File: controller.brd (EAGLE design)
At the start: 150 x 100 mm, 0 parts

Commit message: Firmware added, controller progress
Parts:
- added C1, C2: 18pF, rcl:C0603
- added C10, C11, C12, C18, C19, C20, C21, C22, C3, C4, C5, C6, C7, C8, C9: 0.1µF, rcl:C0603
- added C13, C14, C15: 100µF, rcl:PANASONIC_D
- added C16, C17: 10µF, rcl:C0805
- added J1: SATA0010225X, BW-Connectors:SATA0010225X
- added J10: ALED_A, BW-Connectors:B3B-XH-A
- added J11: ALED_B, BW-Connectors:B3B-XH-A
- added J12: ALED_C, BW-Connectors:B3B-XH-A
- added J13: FRONT_PANEL, pinhead:1X05
- added J14: 12V, pinhead:2X05
- added J15: 5V, pinhead:2X10
- added J16: 3.3V, pinhead:2X02
- added J2: USB, pinhead:1X04
- added J3: ICSP, BW-Connectors:5PIN-1.27
- added J4: PUMP, BW-Connectors:47053-1000
- added J5: FANS, BW-Connectors:47053-1000
- added J6: FLOW, BW-Connectors:22-23-2032
- added J7: TEMP, pinhead:1X02
- added J8: TACH_OUT, BW-Connectors:22-23-2032
- added J9: SHUTDOWN, pinhead:1X02
- added LS1: AI-1224-TWT-5V-R, BW-Active:AI-1224-TWT-5V-R
- added Q1, Q2, Q3, Q4, Q5, Q6, Q7, Q8: NMOSL, BW-Active:SOT23
- added R1, R10, R13, R15: 10kΩ, resistor:R0603
- added R11, R6: 4.7kΩ, resistor:R0603
- added R12, R14, R3, R4: ?, resistor:R0603
- added R2, R5: 1kΩ, resistor:R0603
- added R7, R8, R9: 100kΩ, resistor:R0603
- added SJ1: GNDLINK, jumper:SJ
- added SW1: RESET, BW-PassiveMechanical:TL3305_MICROSWITCH
- added U1: PIC32MZ-EF-144, BW-Active:LQFP144-20X20
- added U2: NCP5501DT33, BW-Active:DPAK
- added U3: MAX6071A_30, BW-Active:SOT23-6L
- added U4: TXU0104, BW-Active:TSSOP14
- added U5: CPC1006N, BW-Active:CPC1006N
- added Y1: 24MHz, BW-PassiveMechanical:HC49/4HSMX
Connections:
- new net !MCLR: J3.1, R2.1, U1.20
- new net !MCLR!_FILTER: C3.1, R1.1, R2.2, SW1.1, SW1.2
- new net 12V: C15.+, J1.P13, J1.P14, J1.P15, J14.1, J14.3, J14.5, J14.7, J14.9, J4.2, J5.2
- new net 3.3V: C10.1, C11.1, C12.1, C13.+, C17.1, C21.1, C4.1, C5.1, C6.1, C7.1, C8.1, C9.1, J16.1, J16.3, J3.2, R1.2, U1.107, U1.122, U1.137, U1.18, U1.33, U1.41, U1.55, U1.64, U1.74, U1.88, U2.3, U4.1
- new net 3V_REF: C20.1, R6.2, U1.40, U3.5, U3.6
- new net 5V: C14.+, C22.1, J1.P7, J1.P8, J1.P9, J10.3, J11.3, J12.3, J15.1, J15.11, J15.13, J15.15, J15.17, J15.19, J15.3, J15.5, J15.7, J15.9, J6.2, LS1.+, R10.2, R11.2, R12.1, R13.2, R14.1, R15.2, R5.2, U4.14
- new net 5V_USB: C16.1, C19.1, J13.1, J2.1, R7.2, R8.2, R9.2, U1.73, U2.1, U3.3, U3.4
- new net ALED_A: J10.2, U4.13
- new net ALED_A_RAW: U1.104, U4.2
- new net ALED_B: J11.2, U4.12
- new net ALED_B_RAW: U1.109, U4.3
- new net ALED_C: J12.2, U4.11
- new net ALED_C_RAW: U1.110, U4.4
- new net ALED_OE: U1.103, U4.8
- new net BUZZER_EN: Q2.1, U1.9
- new net BUZZER_L: LS1.-, Q2.3
- new net EMERGENCY_SD_C1: J9.1, U5.4
- new net EMERGENCY_SD_C2: J9.2, U5.3
- new net EMERGENCY_SD_DRIVE+: R11.1, U5.1
- new net EMERGENCY_SD_DRIVE-: Q8.3, U5.2
- new net EMERGENCY_SD_TRIGGER: Q8.1, U1.10
- new net FAN_PWM: J5.4, Q6.3, R14.2
- new net FAN_PWM_DRIVE: Q6.1, U1.15
- new net FAN_TACH: Q7.3, U1.16
- new net FAN_TACH_RAW: J5.3, Q7.1, R15.1
- new net FLOW_TACH: Q1.3, U1.23
- new net FLOW_TACH_RAW: J6.3, Q1.1, R10.1
- new net FPLED_!B: J13.4, R9.1, U1.98
- new net FPLED_!G: J13.3, R8.1, U1.97
- new net FPLED_!R: J13.2, R7.1, U1.96
- new net GND: C1.1, C10.2, C11.2, C12.2, C13.-, C14.-, C15.-, C16.2, C17.2, C18.2, C19.2, C2.1, C20.2, C21.2, C22.2, C3.2, C4.2, C5.2, C6.2, C7.2, C8.2, C9.2, J1.P10, J1.P12, J1.P4, J1.P5, J1.P6, J10.1, J11.1, J12.1, J13.5, J14.10, J14.2, J14.4, J14.6, J14.8, J15.10, J15.12, J15.14, J15.16, J15.18, J15.2, J15.20, J15.4, J15.6, J15.8, J16.2, J16.4, J2.4, J3.3, J4.1, J5.1, J6.1, J7.2, Q1.2, Q2.2, Q3.2, Q4.2, Q5.2, Q6.2, Q7.2, Q8.2, SJ1.2, SW1.3, SW1.4, U1.108, U1.123, U1.136, U1.17, U1.32, U1.42, U1.54, U1.63, U1.75, U1.89, U2.TAB, U3.1, U3.2, U4.7
- new net OSC1: C2.2, R3.2, U1.71, Y1.2
- new net OSC2: R4.1, U1.72
- new net OSC2_R: C1.2, R3.1, R4.2, Y1.1
- new net PGEC: J3.5, U1.35
- new net PGED: J3.4, U1.36
- new net POWER_SENSE: R5.1, U1.46
- new net PUMP_PWM: J4.4, Q4.3, R12.2
- new net PUMP_PWM_DRIVE: Q4.1, U1.12
- new net PUMP_TACH: Q5.3, U1.14
- new net PUMP_TACH_RAW: J4.3, Q5.1, R13.1
- new net TACH_OUT: J8.3, Q3.3
- new net TACH_OUT_DRIVE: Q3.1, U1.11
- new net TACH_OUT_GNDLINK: J8.1, SJ1.1
- new net TEMP_SENSE: C18.1, J7.1, R6.1, U1.25
- new net USB_D+: J2.3, U1.77
- new net USB_D-: J2.2, U1.76

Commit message: Controller (hopefully) finished
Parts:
- added A1: VXO7805-500, BW-Active:VXO78-500
- added C23, C27: 0.1µF, rcl:C0603
- added C24: 22µF, rcl:C0603
- added C25: 10µF, rcl:C0805
- added C26: 100µF, rcl:PANASONIC_D
- added D1, D2: GS1A-L, BW-Active:DO-214AC
- added J17: 12V_WD, pinhead:1X02
- added K1: G5Q-1, BW-PassiveMechanical:G5Q-1
- added Q10, Q9: PMOS, BW-Active:SOT23
- added Q11: NMOSL, BW-Active:SOT23
- added R16, R18: 1kΩ, resistor:R0603
- added R17: 10kΩ, resistor:R0603
- added TP1, TP10, TP11, TP12, TP14, TP15, TP2, TP3, TP4, TP5, TP6, TP7, TP8, TP9: RCU-0(J), BW-PassiveMechanical:TP_0603_JOINED
- moved Q8 536.6 mm to (73.8, 58.7), flipped to the bottom, turned to 180 degrees
- moved J15 517.1 mm to (14.6, 59.7), turned to 180 degrees
- moved R15 504.1 mm to (38.9, 58.5), flipped to the bottom, turned to 270 degrees
- moved J14 504.0 mm to (20.0, 53.5), turned to 180 degrees
- moved Q7 501.0 mm to (41.7, 62.1), flipped to the bottom, turned to 90 degrees
- moved R14 490.3 mm to (45.5, 57.5), flipped to the bottom, turned to 90 degrees
- moved Q6 487.0 mm to (45.8, 61.2), flipped to the bottom
- moved R13 476.0 mm to (50.2, 56.1), flipped to the bottom, turned to 180 degrees
- moved J16 474.1 mm to (15.0, 14.5)
- moved Q5 465.3 mm to (46.9, 53.0), flipped to the bottom, turned to 270 degrees
- moved SJ1 463.7 mm to (70.2, 65.6), turned to 180 degrees
- moved R12 462.2 mm to (50.2, 56.1), turned to 180 degrees
- moved Q4 453.3 mm to (46.6, 54.9)
- moved R11 441.8 mm to (78.5, 54.7), turned to 270 degrees
- moved Q3 440.5 mm to (51.0, 53.0), turned to 270 degrees
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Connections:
- new net 12V_PUMP: J4.2, K1.2
- new net 12V_PUMP_WD: K1.4, Q10.3
- new net 12V_WD: A1.1, C25.1, C26.+, Q10.2, Q9.2, R17.2
- new net 12V_WD_PROTECT: Q9.1, R16.1
- new net 12V_WD_RAW: J17.1, Q9.3
- new net 5V_SB: C16.1, C19.1, D1.C, D2.C, J13.1, R12.1, R13.2, R7.2, R8.2, R9.2, TP5.1, U2.1, U3.3, U3.4
- new net 5V_WD: A1.3, C24.1, D2.A, R18.2
- new net PUMP_WD_DRIVE: Q10.1, Q11.3, R17.1
- new net PUMP_WD_RUN: Q11.1, U1.8
- new net WD_DETECT: R18.1, U1.81
- net 12V: now also K1.1, K1.3; no longer J4.2
- net 3.3V: now also C27.1
- net 3V_REF: now also TP6.1
- net 5V: no longer R12.1, R13.2
- net 5V_USB: now also C23.1, D1.A, TP4.1; no longer C16.1, C19.1, J13.1, R7.2, R8.2, R9.2, U2.1, U3.3, U3.4
- net ALED_A: now also TP1.1
- net ALED_B: now also TP2.1
- net ALED_C: now also TP3.1
- net ALED_OE: now also TP15.1
- net FAN_PWM: now also TP14.1
- net FAN_TACH: now also TP12.1
- net FLOW_TACH: now also TP8.1
- net GND: now also A1.2, C23.2, C24.2, C25.2, C26.-, C27.2, J17.2, K1.5, Q11.2, R16.2
- net PUMP_PWM: now also TP11.1
- net PUMP_TACH: now also TP10.1
- net TACH_OUT: now also TP9.1
- net TEMP_SENSE: now also TP7.1
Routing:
- net 5V: track 0.00 -> 264.4 mm
- net 3.3V: track 0.00 -> 150.2 mm, vias 0 -> 13
- net 5V_SB: track 0.00 -> 141.4 mm, vias 0 -> 8
- net 12V: track 0.00 -> 105.8 mm
- net 12V_WD: track 0.00 -> 75.1 mm, vias 0 -> 5
- net GND: track 0.00 -> 46.9 mm, vias 0 -> 128
- net BUZZER_EN: track 0.00 -> 36.1 mm, vias 0 -> 1
- net EMERGENCY_SD_TRIGGER: track 0.00 -> 35.8 mm, vias 0 -> 1
- net PUMP_WD_RUN: track 0.00 -> 26.2 mm, vias 0 -> 1
- net ALED_OE: track 0.00 -> 24.3 mm, vias 0 -> 1
- net !MCLR: track 0.00 -> 23.8 mm
- net TEMP_SENSE: track 0.00 -> 22.6 mm
- net ALED_B: track 0.00 -> 21.6 mm, vias 0 -> 1
- net TACH_OUT: track 0.00 -> 21.2 mm, vias 0 -> 1
- net FAN_PWM_DRIVE: track 0.00 -> 20.8 mm, vias 0 -> 1
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- added copper zone on layer 1, net GND
- added copper zone on layer 16, net GND
- added copper zone on layer 1, net LOGO
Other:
- board size 150 x 100 mm -> 81 x 70 mm
- board text added: "+"
- board text added: "+ -"
- board text added: "- +"
- board text added: "JLCJLCJLCJLC"
- board text added: "©2022 BlockWorker blockworker.de"

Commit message: Parts Ordered
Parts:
- R11: value 4.7kΩ -> 2kΩ
- U4: value TXU0104 -> TXU0304-3
- U5: value CPC1006N -> CPC1017N; device BW-Active:CPC1006N -> BW-Active:CPC10*N
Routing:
- net GND: vias 128 -> 155
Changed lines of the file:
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@@
 <setting verticaltext="up"/>
 </settings>
-<grid distance="0.02" unitdist="mm" unit="mm" style="lines" multiple="1" display="no" altdistance="0.1" altunitdist="mm" altunit="mm"/>
+<grid distance="1" unitdist="mm" unit="mm" style="lines" multiple="1" display="no" altdistance="0.1" altunitdist="mm" altunit="mm"/>
 <layers>
 <layer number="1" name="Top" color="4" fill="1" visible="yes" active="yes"/>
@@
 </layers>
 <board>
+<fusionsync huburn="a.cGVyc29uYWw6dWUyYmY1N2E4" projecturn="a.cGVyc29uYWw6dWUyYmY1N2E4IzIwMjIwMTIwNDg3Nzg3NTgx" f3durn="urn:adsk.wipprod:dm.lineage:FNo4Y8BsTfObfx8X_7kaJQ" pcbguid="" lastpulledtime="" lastsyncedchangeguid="" latestrevisionid="456a566e-ee09-4212-9d23-57c6c17b9b97" lastsyncedrevisionid="456a566e-ee09-4212-9d23-57c6c17b9b97" lastboardhashguid="7ab29c69-62af-bade-653a-f237d7fa49a6" lastpushedtime="2022-02-19T19:35:36Z" linktopcb3d="true"/>
 <plain>
 <wire x1="0" y1="0" x2="81" y2="0" width="0" layer="20"/>
@@
 <attribute name="VALUE" x="28.065" y="45.195" size="1.016" layer="27" font="vector" ratio="15"/>
 </element>
-<element name="U4" library="BW-Active" library_urn="urn:adsk.eagle:library:33783073" package="TSSOP14" package3d_urn="urn:adsk.eagle:package:33783235/2" value="TXU0104" x="57" y="23.5" smashed="yes" rot="MR90">
+<element name="U4" library="BW-Active" library_urn="urn:adsk.eagle:library:33783073" package="TSSOP14" package3d_urn="urn:adsk.eagle:package:33783235/2" value="TXU0304-3" x="57" y="23.5" smashed="yes" rot="MR90">
 <attribute name="NAME" x="55.6828" y="19.5956" size="1.016" layer="26" font="vector" ratio="15" rot="MR0"/>
 <attribute name="VALUE" x="60.1828" y="26.4138" size="1.016" layer="28" font="vector" ratio="15" rot="MR0"/>
@@
 <attribute name="VALUE" x="69.925" y="33.895" size="1.016" layer="28" font="vector" ratio="15" rot="MR90"/>
 </element>
-<element name="U5" library="BW-Active" library_urn="urn:adsk.eagle:library:33783073" package="CPC1006N" package3d_urn="urn:adsk.eagle:package:33936582/2" value="CPC1006N" x="74" y="52.5" smashed="yes" rot="R270">
+<element name="U5" library="BW-Active" library_urn="urn:adsk.eagle:library:33783073" package="CPC10*N" package3d_urn="urn:adsk.eagle:package:33936582/3" value="CPC1017N" x="74" y="52.5" smashed="yes" rot="R270">
 <attribute name="NAME" x="74.56" y="48.56" size="1.016" layer="25" font="vector" ratio="15" rot="R90"/>
 <attribute name="VALUE" x="77.456" y="49.833" size="1.016" layer="27" font="vector" ratio="15" rot="R90"/>
 </element>
-<element name="R11" library="resistor" library_urn="urn:adsk.eagle:library:348" package="R0603" package3d_urn="urn:adsk.eagle:package:23555/3" value="4.7kΩ" x="78.5" y="54.7" smashed="yes" rot="R270">
+<element name="R11" library="resistor" library_urn="urn:adsk.eagle:library:348" package="R0603" package3d_urn="urn:adsk.eagle:package:23555/3" value="2kΩ" x="78.5" y="54.7" smashed="yes" rot="R270">
 <attribute name="NAME" x="78.065" y="56.535" size="1.016" layer="25" font="vector" ratio="15"/>
 <attribute name="VALUE" x="80.605" y="52.565" size="1.016" layer="27" font="vector" ratio="15" rot="R90"/>
@@
 <wire x1="31.63" y1="29.75" x2="30.25" y2="29.75" width="0.1524" layer="1"/>
 <wire x1="32.1" y1="29.28" x2="31.63" y2="29.75" width="0.1524" layer="1"/>
-<via x="32.15" y="25.6" extent="1-16" drill="0.3"/>
-<wire x1="32.15" y1="25.6" x2="32.28" y2="25.6" width="0.1524" layer="1"/>
+<via x="32.23" y="25.6" extent="1-16" drill="0.3"/>
+<wire x1="32.23" y1="25.6" x2="32.28" y2="25.6" width="0.1524" layer="1"/>
 <wire x1="32.75" y1="25.13" x2="32.75" y2="23.75" width="0.1524" layer="1"/>
 <wire x1="32.28" y1="25.6" x2="32.75" y2="25.13" width="0.1524" layer="1"/>
@@
 <wire x1="49.9" y1="40.22" x2="50.37" y2="39.75" width="0.1524" layer="1"/>
 <wire x1="20.714" y1="13.45" x2="20.714" y2="17.954" width="0.254" layer="1"/>
-<wire x1="30.65" y1="24.1" x2="32.15" y2="25.6" width="0.254" layer="1"/>
+<wire x1="32.23" y1="25.54" x2="32.23" y2="25.6" width="0.254" layer="1"/>
+<wire x1="32.23" y1="25.54" x2="30.79" y2="24.1" width="0.254" layer="1"/>
 <wire x1="20.714" y1="17.954" x2="22.44" y2="19.68" width="0.254" layer="1"/>
 <wire x1="22.44" y1="19.68" x2="25.76" y2="19.68" width="0.254" layer="1"/>
 <wire x1="25.76" y1="19.68" x2="30.18" y2="24.1" width="0.254" layer="1"/>
-<wire x1="30.18" y1="24.1" x2="30.65" y2="24.1" width="0.254" layer="1"/>
-<wire x1="32.15" y1="25.6" x2="32.1" y2="25.65" width="0.254" layer="1"/>
-<wire x1="32.1" y1="25.65" x2="32.1" y2="26.68" width="0.254" layer="1"/>
-<wire x1="32.1" y1="26.68" x2="32.1" y2="29.15" width="0.254" layer="1"/>
-<wire x1="32.1" y1="26.68" x2="39.15" y2="26.68" width="0.254" layer="1"/>
+<wire x1="30.18" y1="24.1" x2="30.79" y2="24.1" width="0.254" layer="1"/>
+<wire x1="32.2" y1="26.68" x2="32.2" y2="25.63" width="0.254" layer="1"/>
+<wire x1="32.23" y1="25.6" x2="32.2" y2="25.63" width="0.254" layer="1"/>
+<wire x1="32.2" y1="29.05" x2="32.1" y2="29.15" width="0.254" layer="1"/>
+<wire x1="32.2" y1="29.05" x2="32.2" y2="26.68" width="0.254" layer="1"/>
+<wire x1="32.2" y1="26.68" x2="39.15" y2="26.68" width="0.254" layer="1"/>
 <wire x1="39.15" y1="25.6" x2="39.15" y2="26.68" width="0.254" layer="1"/>
 <wire x1="39.15" y1="26.68" x2="48.15" y2="26.68" width="0.254" layer="1"/>
@@
 <wire x1="32.1" y1="33.65" x2="33.15" y2="33.65" width="0.254" layer="1"/>
 <wire x1="33.15" y1="33.65" x2="33.16" y2="33.66" width="0.254" layer="1"/>
+<wire x1="32.15" y1="25.6" x2="32.23" y2="25.6" width="0.1524" layer="16"/>
 </signal>
 <signal name="GND">
@@
 <via x="33.9" y="53.9" extent="1-16" drill="0.3"/>
 <via x="39.4" y="47.3" extent="1-16" drill="0.3"/>
+<via x="53.7" y="53.4" extent="1-16" drill="0.3"/>
+<via x="50" y="50.1" extent="1-16" drill="0.3"/>
+<via x="21.4" y="44.1" extent="1-16" drill="0.3"/>
+<via x="22.2" y="47.6" extent="1-16" drill="0.3"/>
+<via x="14.6" y="32.2" extent="1-16" drill="0.3"/>
+<via x="13.7" y="32.2" extent="1-16" drill="0.3"/>
+<via x="19" y="33.3" extent="1-16" drill="0.3"/>
+<via x="14" y="33.2" extent="1-16" drill="0.3"/>
+<via x="17.1" y="3.5" extent="1-16" drill="0.3"/>
+<via x="12.4" y="4.8" extent="1-16" drill="0.3"/>
+<via x="17.7" y="4.8" extent="1-16" drill="0.3"/>
+<via x="27.2" y="4.5" extent="1-16" drill="0.3"/>
+<via x="18.9" y="7.8" extent="1-16" drill="0.3"/>
+<via x="27" y="7.3" extent="1-16" drill="0.3"/>
+<via x="42.3" y="4.8" extent="1-16" drill="0.3"/>
+<via x="43.2" y="3.5" extent="1-16" drill="0.3"/>
+<via x="28.5" y="44.3" extent="1-16" drill="0.3"/>
+<via x="27.6" y="45.8" extent="1-16" drill="0.3"/>
+<via x="26" y="45" extent="1-16" drill="0.3"/>
+<via x="28.4" y="40" extent="1-16" drill="0.3"/>
+<via x="41.2" y="47.4" extent="1-16" drill="0.3"/>
+<via x="53.7" y="39.2" extent="1-16" drill="0.3"/>
+<via x="53.7" y="32.7" extent="1-16" drill="0.3"/>
+<via x="50.7" y="23.2" extent="1-16" drill="0.3"/>
+<via x="40.2" y="21.8" extent="1-16" drill="0.3"/>
+<via x="32.9" y="21.8" extent="1-16" drill="0.3"/>
+<via x="47.4" y="49.8" extent="1-16" drill="0.3"/>
 </signal>
 <signal name="!MCLR!_FILTER">
@@
 </note>
 <note version="8.3" severity="warning">
+Since Version 8.3, EAGLE supports Fusion synchronisation.
+This feature will not be available in this version and saving
+the document will break the link to the Fusion PCB feature.
+</note>
+<note version="8.3" severity="warning">

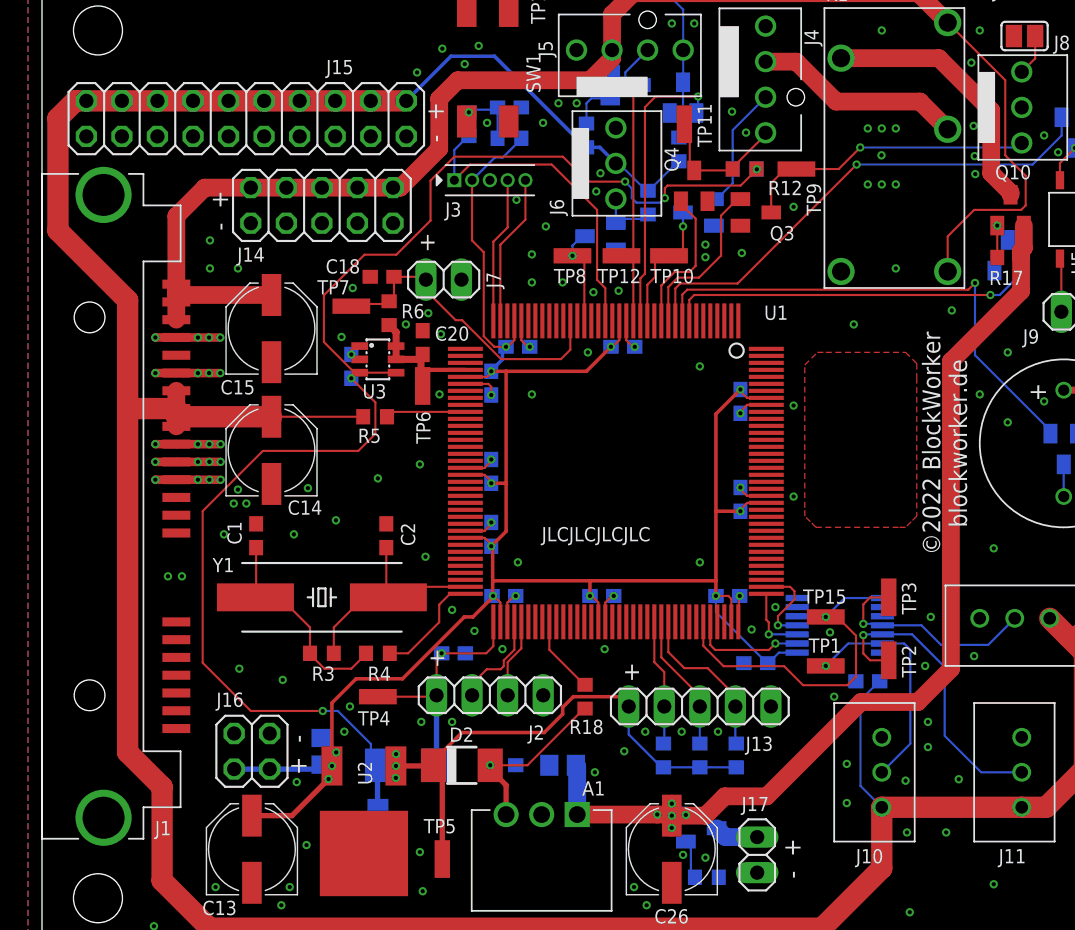
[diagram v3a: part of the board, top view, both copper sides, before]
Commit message: Replaced MCU footprint due to earlier error
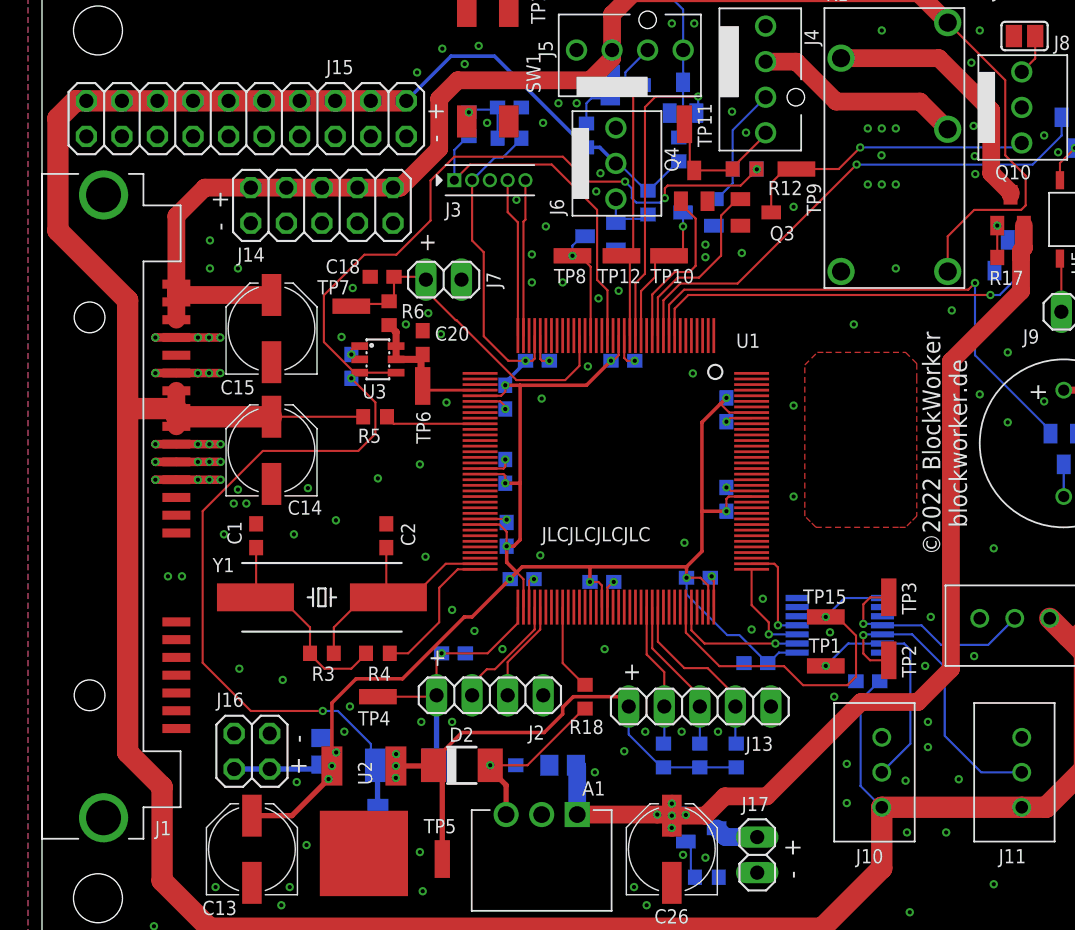
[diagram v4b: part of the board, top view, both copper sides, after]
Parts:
- U1: value PIC32MZ-EF-144 -> PIC32MZ-EF-144PH; device BW-Active:LQFP144-20X20 -> BW-Active:TQFP144-16X16
- moved C11 2.47 mm to (46.9, 26.9)
- moved C9 1.77 mm to (34.3, 26.8)
- moved C5 1.72 mm to (35.4, 42.4)
- moved C6 1.41 mm to (33.1, 39.8)
- moved C27 1.17 mm to (48.9, 38.9)
- moved C8 1.10 mm to (33.2, 30.0)
- moved C10 1.00 mm to (40.0, 26.6)
- moved C12 1.00 mm to (48.9, 32.5)
- moved C4 1.00 mm to (41.5, 42.4)
- moved C7 1.00 mm to (33.1, 34.5)
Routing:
- net 3.3V: track 150.3 -> 152.9 mm
- net OSC2: track 7.90 -> 10.4 mm
- net ALED_B_RAW: track 4.99 -> 7.18 mm
- net 5V_USB: track 18.1 -> 19.9 mm
- net ALED_OE: track 24.3 -> 26.0 mm
- net OSC1: track 16.0 -> 17.8 mm
- net PUMP_WD_RUN: track 26.2 -> 27.9 mm
- net USB_D+: track 5.66 -> 7.27 mm
- net BUZZER_EN: track 36.1 -> 37.7 mm
- net TEMP_SENSE: track 22.6 -> 24.1 mm
- net USB_D-: track 7.08 -> 8.49 mm
- net ALED_A_RAW: track 8.20 -> 9.60 mm
- net EMERGENCY_SD_TRIGGER: track 35.8 -> 37.2 mm
- net FPLED_!B: track 11.7 -> 13.0 mm
- net TACH_OUT_DRIVE: track 11.8 -> 13.2 mm
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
